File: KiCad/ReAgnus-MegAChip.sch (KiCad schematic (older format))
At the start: 19 parts, among them J3 Conn_02x01, J4 Conn_01x01, J5 Conn_01x01, J6 Conn_01x01, J7 Conn_01x01, U1 PLCC-84-Plug, U2 LM1117-3.3, U3 SN74CBTD16210, U4 SN74CBTD16210, U5 SN74CBTD16210, U6 SN74CBTD16210, U9 Agnus_TH_plug_pins

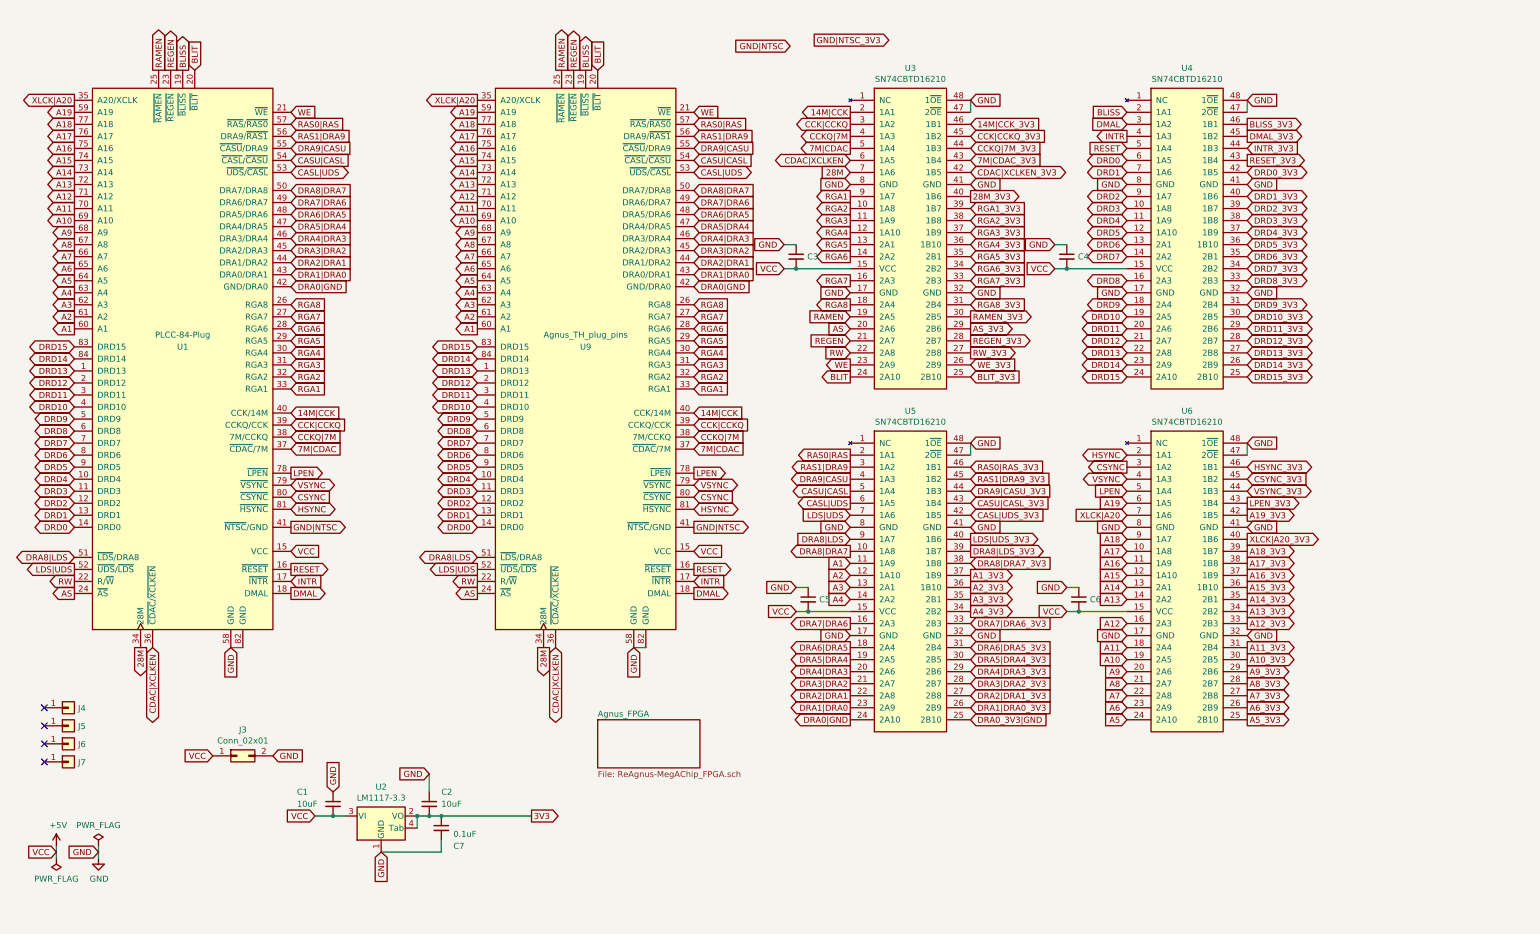
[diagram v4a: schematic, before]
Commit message: added 74LVC1G07 buffer with open-drain output
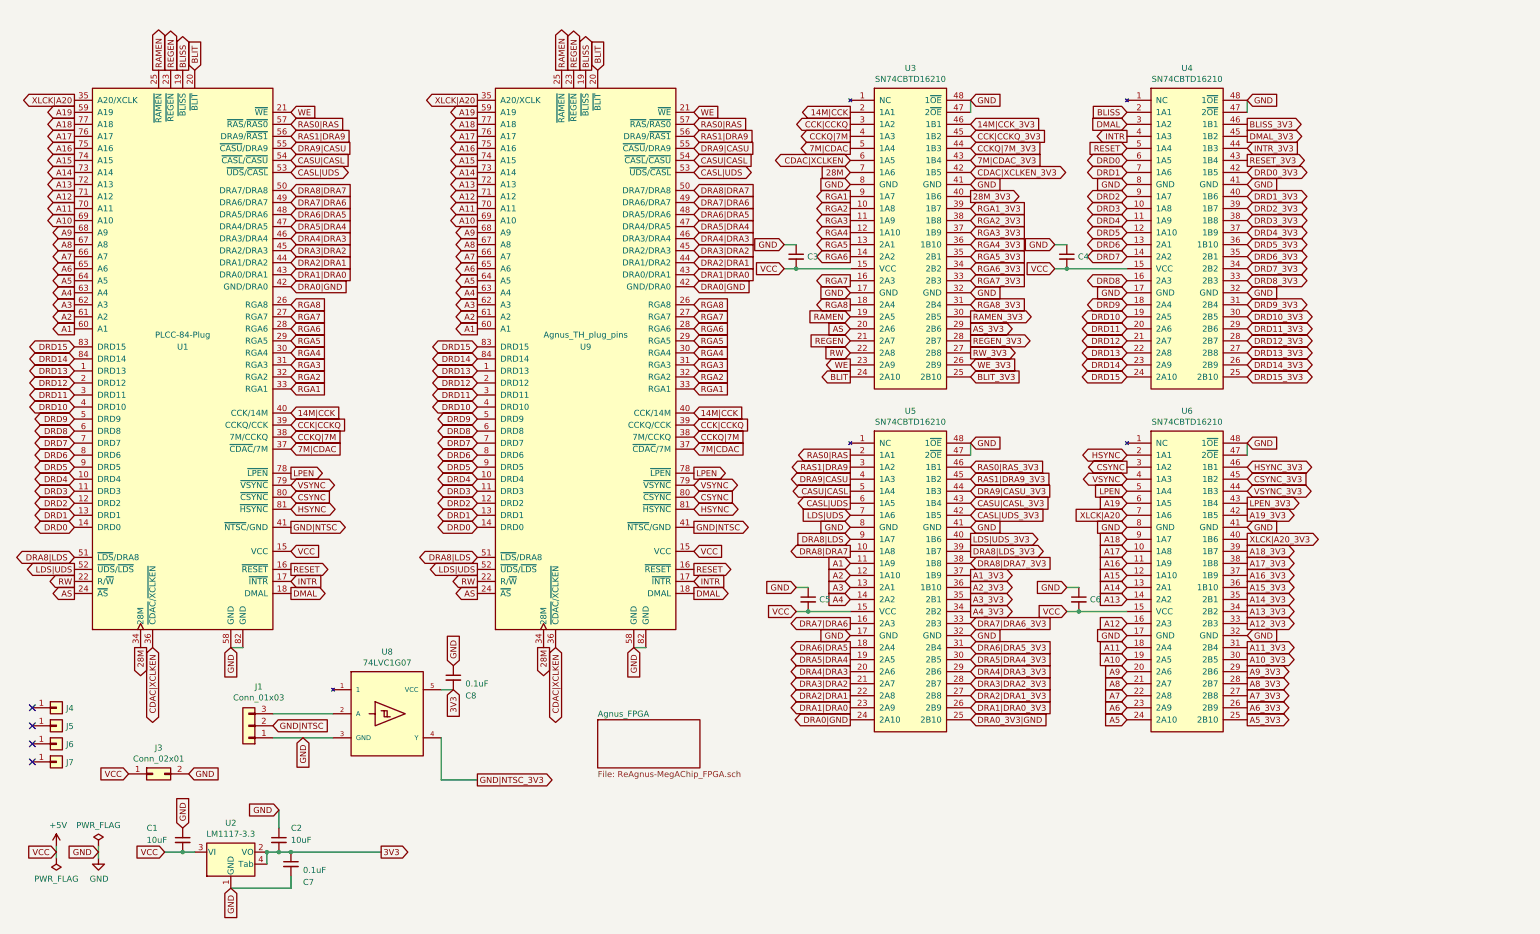
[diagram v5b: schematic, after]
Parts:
- added C8: 0.1uF, Capacitor_SMD:C_0805_2012Metric_Pad1.15x1.40mm_HandSolder, symbol Device:C_Small
- added J1: Conn_01x03, Connector_PinHeader_2.54mm:PinHeader_1x03_P2.54mm_Vertical, symbol Connector_Generic:Conn_01x03
- added U8: 74LVC1G07, Agnus:SOT-353_SC-70-5_Custom_Handsoldering, symbol ReAgnus-MegAChip:74LVC1G07
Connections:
- net 3V3: now also C8.2, U8.5 (VCC)
- net GND: now also C8.1, J1.1 (Pin_1), U8.3 (GND)
- net GND|NTSC: now also J1.2 (Pin_2)
- net GND|NTSC_3V3: now also U8.4 (Y)
- new net: J1.3 (Pin_3), U8.2 (A)
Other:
- moved on the sheet: C1, C2, C7, J3, J4, J5, J6, J7, U2
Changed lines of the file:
@@
 L Connector_Generic:Conn_01x01 J4
 U 1 1 60D1FBEB
-P 950 6200
-F 0 "J4" H 1030 6196 50  0000 L CNN
-F 1 "Conn_01x01" H 1030 6151 50  0001 L CNN
-F 2 "Connector_PinHeader_2.54mm:PinHeader_1x01_P2.54mm_Vertical" H 950 6200 50  0001 C CNN
-F 3 "~" H 950 6200 50  0001 C CNN
-	1    950  6200
+P 850 6200
+F 0 "J4" H 930 6196 50  0000 L CNN
+F 1 "Conn_01x01" H 930 6151 50  0001 L CNN
+F 2 "Connector_PinHeader_2.54mm:PinHeader_1x01_P2.54mm_Vertical" H 850 6200 50  0001 C CNN
+F 3 "~" H 850 6200 50  0001 C CNN
+	1    850  6200
 	1    0    0    -1
 $EndComp
@@
 L Connector_Generic:Conn_01x01 J5
 U 1 1 60D20CDD
-P 950 6350
-F 0 "J5" H 1030 6346 50  0000 L CNN
-F 1 "Conn_01x01" H 1030 6301 50  0001 L CNN
-F 2 "Connector_PinHeader_2.54mm:PinHeader_1x01_P2.54mm_Vertical" H 950 6350 50  0001 C CNN
-F 3 "~" H 950 6350 50  0001 C CNN
-	1    950  6350
+P 850 6350
+F 0 "J5" H 930 6346 50  0000 L CNN
+F 1 "Conn_01x01" H 930 6301 50  0001 L CNN
+F 2 "Connector_PinHeader_2.54mm:PinHeader_1x01_P2.54mm_Vertical" H 850 6350 50  0001 C CNN
+F 3 "~" H 850 6350 50  0001 C CNN
+	1    850  6350
 	1    0    0    -1
 $EndComp
@@
 L Connector_Generic:Conn_01x01 J6
 U 1 1 60D21648
-P 950 6500
-F 0 "J6" H 1030 6496 50  0000 L CNN
-F 1 "Conn_01x01" H 1030 6451 50  0001 L CNN
-F 2 "Connector_PinHeader_2.54mm:PinHeader_1x01_P2.54mm_Vertical" H 950 6500 50  0001 C CNN
-F 3 "~" H 950 6500 50  0001 C CNN
-	1    950  6500
+P 850 6500
+F 0 "J6" H 930 6496 50  0000 L CNN
+F 1 "Conn_01x01" H 930 6451 50  0001 L CNN
+F 2 "Connector_PinHeader_2.54mm:PinHeader_1x01_P2.54mm_Vertical" H 850 6500 50  0001 C CNN
+F 3 "~" H 850 6500 50  0001 C CNN
+	1    850  6500
 	1    0    0    -1
 $EndComp
@@
 L Connector_Generic:Conn_01x01 J7
 U 1 1 60D21D5E
-P 950 6650
-F 0 "J7" H 1030 6646 50  0000 L CNN
-F 1 "Conn_01x01" H 1030 6601 50  0001 L CNN
-F 2 "Connector_PinHeader_2.54mm:PinHeader_1x01_P2.54mm_Vertical" H 950 6650 50  0001 C CNN
-F 3 "~" H 950 6650 50  0001 C CNN
-	1    950  6650
-	1    0    0    -1
-$EndComp
-NoConn ~ 750  6200
-NoConn ~ 750  6350
-NoConn ~ 750  6500
-NoConn ~ 750  6650
+P 850 6650
+F 0 "J7" H 930 6646 50  0000 L CNN
+F 1 "Conn_01x01" H 930 6601 50  0001 L CNN
+F 2 "Connector_PinHeader_2.54mm:PinHeader_1x01_P2.54mm_Vertical" H 850 6650 50  0001 C CNN
+F 3 "~" H 850 6650 50  0001 C CNN
+	1    850  6650
+	1    0    0    -1
+$EndComp
+NoConn ~ 650  6200
+NoConn ~ 650  6350
+NoConn ~ 650  6500
+NoConn ~ 650  6650
 $Comp
 L Connector_Generic:Conn_02x01 J3
 U 1 1 60E54D12
-P 2350 6600
-F 0 "J3" H 2400 6817 50  0000 C CNN
-F 1 "Conn_02x01" H 2400 6726 50  0000 C CNN
-F 2 "Connector_PinHeader_2.54mm:PinHeader_2x01_P2.54mm_Vertical" H 2350 6600 50  0001 C CNN
-F 3 "~" H 2350 6600 50  0001 C CNN
-	1    2350 6600
-	1    0    0    -1
-$EndComp
-Text GLabel 2650 6600 2    50   Input ~ 0
+P 1650 6750
+F 0 "J3" H 1700 6967 50  0000 C CNN
+F 1 "Conn_02x01" H 1700 6876 50  0000 C CNN
+F 2 "Connector_PinHeader_2.54mm:PinHeader_2x01_P2.54mm_Vertical" H 1650 6750 50  0001 C CNN
+F 3 "~" H 1650 6750 50  0001 C CNN
+	1    1650 6750
+	1    0    0    -1
+$EndComp
+Text GLabel 1950 6750 2    50   Input ~ 0
 GND
 Wire Wire Line
@@
 L ReAgnus-MegAChip:LM1117-3.3 U2
 U 1 1 632C9030
-P 3550 7100
-F 0 "U2" H 3550 7342 50  0000 C CNN
-F 1 "LM1117-3.3" H 3550 7251 50  0000 C CNN
-F 2 "Package_TO_SOT_SMD:SOT-223" H 3550 7100 50  0001 C CNN
-F 3 "" H 3550 7100 50  0001 C CNN
-	1    3550 7100
+P 2300 7400
+F 0 "U2" H 2300 7642 50  0000 C CNN
+F 1 "LM1117-3.3" H 2300 7551 50  0000 C CNN
+F 2 "Package_TO_SOT_SMD:SOT-223" H 2300 7400 50  0001 C CNN
+F 3 "" H 2300 7400 50  0001 C CNN
+	1    2300 7400
 	1    0    0    -1
 $EndComp
@@
 Text GLabel 7450 1550 0    50   Output ~ 0
 7M|CDAC
-Text GLabel 7150 650  2    50   Output ~ 0
+Text GLabel 4350 6800 2    50   Output ~ 0
 GND|NTSC_3V3
 Text GLabel 4350 3200 0    50   BiDi ~ 0
@@
 Text GLabel 8450 6300 2    50   Input ~ 0
 DRA0_3V3|GND
-Text GLabel 6950 700  0    50   Input ~ 0
+Text GLabel 2650 6350 2    50   Input ~ 0
 GND|NTSC
-Text GLabel 3000 7100 0    50   Input ~ 0
+Text GLabel 1750 7400 0    50   Input ~ 0
 VCC
-Text GLabel 2150 6600 0    50   Input ~ 0
+Text GLabel 1450 6750 0    50   Input ~ 0
 VCC
-Text GLabel 3150 6900 1    50   Input ~ 0
+Text GLabel 1900 7200 1    50   Input ~ 0
 GND
 $Comp
 L Device:C_Small C2
 U 1 1 63947670
-P 3950 7000
+P 2700 7300
 AR Path="/63947670" Ref="C2"  Part="1"
 AR Path="/632D3BDF/63947670" Ref="C?"  Part="1"
 AR Path="/632F104D/63947670" Ref="C?"  Part="1"
-F 0 "C2" H 4050 7100 50  0000 L CNN
-F 1 "10uF" H 4050 7000 50  0000 L CNN
-F 2 "Capacitor_SMD:C_1206_3216Metric_Pad1.42x1.75mm_HandSolder" H 3950 7000 50  0001 C CNN
-F 3 "~" H 3950 7000 50  0001 C CNN
-	1    3950 7000
+F 0 "C2" H 2800 7400 50  0000 L CNN
+F 1 "10uF" H 2800 7300 50  0000 L CNN
+F 2 "Capacitor_SMD:C_1206_3216Metric_Pad1.42x1.75mm_HandSolder" H 2700 7300 50  0001 C CNN
+F 3 "~" H 2700 7300 50  0001 C CNN
+	1    2700 7300
 	1    0    0    -1
 $EndComp
@@
 L Device:C_Small C1
 U 1 1 63949338
-P 3150 7000
+P 1900 7300
 AR Path="/63949338" Ref="C1"  Part="1"
 AR Path="/632D3BDF/63949338" Ref="C?"  Part="1"
 AR Path="/632F104D/63949338" Ref="C?"  Part="1"
-F 0 "C1" H 2850 7100 50  0000 L CNN
-F 1 "10uF" H 2850 7000 50  0000 L CNN
-F 2 "Capacitor_SMD:C_1206_3216Metric_Pad1.42x1.75mm_HandSolder" H 3150 7000 50  0001 C CNN
-F 3 "~" H 3150 7000 50  0001 C CNN
-	1    3150 7000
-	1    0    0    -1
-$EndComp
-Wire Wire Line
-	3000 7100 3150 7100
-Connection ~ 3150 7100
-Wire Wire Line
-	3150 7100 3250 7100
-Text GLabel 3950 6750 0    50   Input ~ 0
-GND
-Wire Wire Line
-	3850 7100 3950 7100
-Wire Wire Line
-	3850 7200 3850 7100
-Connection ~ 3850 7100
-Text GLabel 4800 7100 2    50   Output ~ 0
+F 0 "C1" H 1600 7400 50  0000 L CNN
+F 1 "10uF" H 1600 7300 50  0000 L CNN
+F 2 "Capacitor_SMD:C_1206_3216Metric_Pad1.42x1.75mm_HandSolder" H 1900 7300 50  0001 C CNN
+F 3 "~" H 1900 7300 50  0001 C CNN
+	1    1900 7300
+	1    0    0    -1
+$EndComp
+Wire Wire Line
+	1750 7400 1900 7400
+Connection ~ 1900 7400
+Wire Wire Line
+	1900 7400 2000 7400
+Text GLabel 2700 7050 0    50   Input ~ 0
+GND
+Wire Wire Line
+	2600 7400 2700 7400
+Wire Wire Line
+	2600 7500 2600 7400
+Connection ~ 2600 7400
+Text GLabel 3550 7400 2    50   Output ~ 0
 3V3
-Connection ~ 3950 7100
-Wire Wire Line
-	3950 7100 4050 7100
-Text GLabel 3550 7400 3    50   Input ~ 0
+Connection ~ 2700 7400
+Wire Wire Line
+	2700 7400 2800 7400
+Text GLabel 2300 7700 3    50   Input ~ 0
 GND
 $Comp
 L Device:C_Small C7
 U 1 1 63951D9D
-P 4050 7200
+P 2800 7500
 AR Path="/63951D9D" Ref="C7"  Part="1"
 AR Path="/632D3BDF/63951D9D" Ref="C?"  Part="1"
 AR Path="/632F104D/63951D9D" Ref="C?"  Part="1"
-F 0 "C7" H 4150 7050 50  0000 L CNN
-F 1 "0.1uF" H 4150 7150 50  0000 L CNN
-F 2 "Capacitor_SMD:C_0805_2012Metric_Pad1.15x1.40mm_HandSolder" H 4050 7200 50  0001 C CNN
-F 3 "~" H 4050 7200 50  0001 C CNN
-	1    4050 7200
-	1    0    0    -1
-$EndComp
-Connection ~ 4050 7100
-Wire Wire Line
-	4050 7100 4800 7100
-Wire Wire Line
-	3950 6900 3950 6750
-Wire Wire Line
-	4050 7400 4050 7300
-Wire Wire Line
-	3550 7400 4050 7400
+F 0 "C7" H 2900 7350 50  0000 L CNN
+F 1 "0.1uF" H 2900 7450 50  0000 L CNN
+F 2 "Capacitor_SMD:C_0805_2012Metric_Pad1.15x1.40mm_HandSolder" H 2800 7500 50  0001 C CNN
+F 3 "~" H 2800 7500 50  0001 C CNN
+	1    2800 7500
+	1    0    0    -1
+$EndComp
+Connection ~ 2800 7400
+Wire Wire Line
+	2800 7400 3550 7400
+Wire Wire Line
+	2700 7200 2700 7050
+Wire Wire Line
+	2800 7700 2800 7600
+Wire Wire Line
+	2300 7700 2800 7700
+Wire Wire Line
+	4050 6800 4350 6800
+Wire Wire Line
+	4050 6450 4050 6800
+$Comp
+L ReAgnus-MegAChip:74LVC1G07 U8
+U 1 1 631A6F88
+P 3600 6250
+F 0 "U8" H 3600 6765 50  0000 C CNN
+F 1 "74LVC1G07" H 3600 6674 50  0000 C CNN
+F 2 "Agnus:SOT-353_SC-70-5_Custom_Handsoldering" H 4100 7200 50  0001 C CNN
+F 3 "https://www.ti.com/lit/ds/symlink/sn74lvc1g07-q1.pdf" H 4100 7200 50  0001 C CNN
+	1    3600 6250
+	1    0    0    -1
+$EndComp
+$Comp
+L Connector_Generic:Conn_01x03 J1
+U 1 1 631AE53C
+P 2450 6350
+F 0 "J1" H 2368 6025 50  0000 C CNN
+F 1 "Conn_01x03" H 2368 6116 50  0000 C CNN
+F 2 "Connector_PinHeader_2.54mm:PinHeader_1x03_P2.54mm_Vertical" H 2450 6350 50  0001 C CNN
+F 3 "~" H 2450 6350 50  0001 C CNN
+	1    2450 6350
+	-1   0    0    1
+$EndComp
+Wire Wire Line
+	3150 6250 2650 6250
+Wire Wire Line
+	3150 6450 2650 6450
+Text GLabel 2900 6450 3    50   Input ~ 0
+GND
+$Comp
+L Device:C_Small C8
+U 1 1 631B6BE4
+P 4150 5950
+AR Path="/631B6BE4" Ref="C8"  Part="1"
+AR Path="/632D3BDF/631B6BE4" Ref="C?"  Part="1"
+AR Path="/632F104D/631B6BE4" Ref="C?"  Part="1"
+F 0 "C8" H 4250 5800 50  0000 L CNN
+F 1 "0.1uF" H 4250 5900 50  0000 L CNN
+F 2 "Capacitor_SMD:C_0805_2012Metric_Pad1.15x1.40mm_HandSolder" H 4150 5950 50  0001 C CNN
+F 3 "~" H 4150 5950 50  0001 C CNN
+	1    4150 5950
+	1    0    0    -1
+$EndComp
+Text GLabel 4150 6050 3    50   Input ~ 0
+3V3
+Wire Wire Line
+	4050 6050 4150 6050
+Text GLabel 4150 5850 1    50   Input ~ 0
+GND
 $EndSCHEMATC

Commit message: more routing
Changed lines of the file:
@@
 Text GLabel 9750 4600 0    50   Input ~ 0
 XLCK|A20
-Text GLabel 7450 4800 0    50   Input ~ 0
+Text GLabel 7450 4800 0    50   BiDi ~ 0
 DRA8|LDS
-Text GLabel 7450 4600 0    50   Input ~ 0
-LDS|UDS
-Text GLabel 7450 4500 0    50   Output ~ 0
+Text GLabel 7450 4500 0    50   BiDi ~ 0
 CASL|UDS
 Text GLabel 7450 4300 0    50   Output ~ 0
@@
 Text GLabel 8450 4500 2    50   Input ~ 0
 CASU|CASL_3V3
-Text GLabel 8450 4600 2    50   Input ~ 0
+Text GLabel 8450 4600 2    50   BiDi ~ 0
 CASL|UDS_3V3
-Text GLabel 8450 4800 2    50   Output ~ 0
-LDS|UDS_3V3
-Text GLabel 8450 4900 2    50   Output ~ 0
+Text GLabel 8450 4900 2    50   BiDi ~ 0
 DRA8|LDS_3V3
 Text GLabel 8450 5000 2    50   Input ~ 0
@@
 Text GLabel 4150 5850 1    50   Input ~ 0
 GND
+Text GLabel 8450 4800 2    50   Output ~ 0
+LDS|UDS_3V3
+Text GLabel 7450 4600 0    50   Input ~ 0
+LDS|UDS
 $EndSCHEMATC

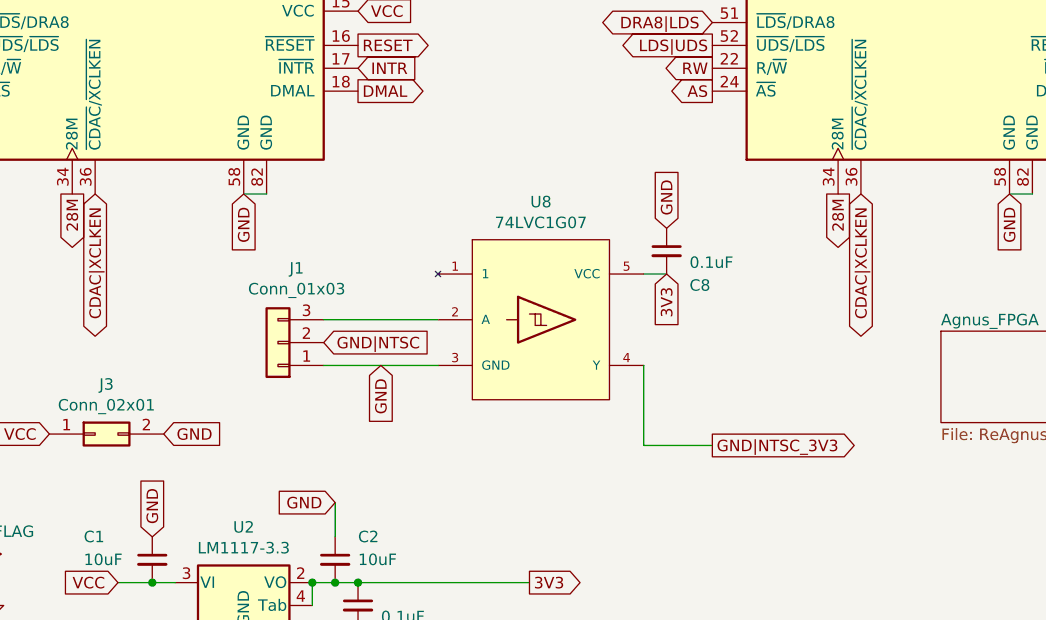
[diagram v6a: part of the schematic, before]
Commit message: added pull-up resistors on PAL/NTSC-line, added JTAG-header
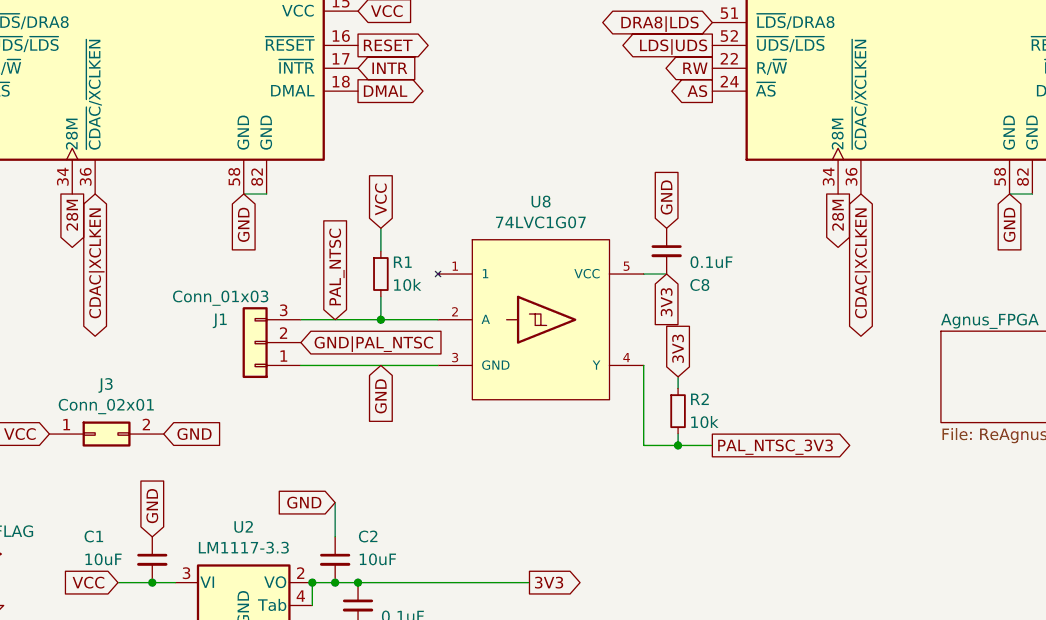
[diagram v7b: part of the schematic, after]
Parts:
- added R1, R2: 10k, Resistor_SMD:R_0603_1608Metric_Pad1.05x0.95mm_HandSolder, symbol Device:R_Small
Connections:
- net +5V: now also R1.1
- net 3V3: now also R2.1
- net GND|NTSC: no longer J1.2 (Pin_2)
- net PAL_NTSC: now reaches J1.3 (Pin_3), U8.2 (A)
- net PAL_NTSC: now also R1.2
- net GND|NTSC_3V3 renamed PAL_NTSC_3V3
- net PAL_NTSC_3V3: now also R2.2
- new net GND|PAL_NTSC: J1.2 (Pin_2)
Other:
- moved on the sheet: J1
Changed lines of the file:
@@
 7M|CDAC
 Text GLabel 4350 6800 2    50   Output ~ 0
-GND|NTSC_3V3
+PAL_NTSC_3V3
 Text GLabel 4350 3200 0    50   BiDi ~ 0
 DRD15
@@
 Text GLabel 8450 6300 2    50   Input ~ 0
 DRA0_3V3|GND
-Text GLabel 2650 6350 2    50   Input ~ 0
-GND|NTSC
+Text GLabel 2550 6350 2    50   Input ~ 0
+GND|PAL_NTSC
 Text GLabel 1750 7400 0    50   Input ~ 0
 VCC
@@
 	2300 7700 2800 7700
 Wire Wire Line
-	4050 6800 4350 6800
+	4050 6800 4200 6800
 Wire Wire Line
 	4050 6450 4050 6800
@@
 L Connector_Generic:Conn_01x03 J1
 U 1 1 631AE53C
-P 2450 6350
-F 0 "J1" H 2368 6025 50  0000 C CNN
-F 1 "Conn_01x03" H 2368 6116 50  0000 C CNN
-F 2 "Connector_PinHeader_2.54mm:PinHeader_1x03_P2.54mm_Vertical" H 2450 6350 50  0001 C CNN
-F 3 "~" H 2450 6350 50  0001 C CNN
-	1    2450 6350
+P 2350 6350
+F 0 "J1" H 2500 6250 50  0000 C CNN
+F 1 "Conn_01x03" H 2500 6150 50  0000 C CNN
+F 2 "Connector_PinHeader_2.54mm:PinHeader_1x03_P2.54mm_Vertical" H 2350 6350 50  0001 C CNN
+F 3 "~" H 2350 6350 50  0001 C CNN
+	1    2350 6350
 	-1   0    0    1
 $EndComp
 Wire Wire Line
-	3150 6250 2650 6250
-Wire Wire Line
-	3150 6450 2650 6450
+	3150 6250 2900 6250
 Text GLabel 2900 6450 3    50   Input ~ 0
 GND
@@
 Text GLabel 7450 4600 0    50   Input ~ 0
 LDS|UDS
+$Comp
+L Device:R_Small R1
+U 1 1 632802A6
+P 2900 6050
+F 0 "R1" H 2950 6100 50  0000 L CNN
+F 1 "10k" H 2950 6000 50  0000 L CNN
+F 2 "Resistor_SMD:R_0603_1608Metric_Pad1.05x0.95mm_HandSolder" H 2900 6050 50  0001 C CNN
+F 3 "~" H 2900 6050 50  0001 C CNN
+	1    2900 6050
+	1    0    0    -1
+$EndComp
+Connection ~ 2900 6250
+Text GLabel 4200 6500 1    50   Input ~ 0
+3V3
+Wire Wire Line
+	2900 6250 2900 6150
+Wire Wire Line
+	2900 5950 2900 5850
+Text GLabel 2700 6250 1    50   Input ~ 0
+PAL_NTSC
+Text GLabel 2900 5850 1    50   Input ~ 0
+VCC
+Wire Wire Line
+	2550 6250 2900 6250
+Wire Wire Line
+	2550 6450 3150 6450
+$Comp
+L Device:R_Small R2
+U 1 1 6328BA47
+P 4200 6650
+F 0 "R2" H 4250 6700 50  0000 L CNN
+F 1 "10k" H 4250 6600 50  0000 L CNN
+F 2 "Resistor_SMD:R_0603_1608Metric_Pad1.05x0.95mm_HandSolder" H 4200 6650 50  0001 C CNN
+F 3 "~" H 4200 6650 50  0001 C CNN
+	1    4200 6650
+	1    0    0    -1
+$EndComp
+Wire Wire Line
+	4200 6500 4200 6550
+Wire Wire Line
+	4200 6750 4200 6800
+Connection ~ 4200 6800
+Wire Wire Line
+	4200 6800 4350 6800
 $EndSCHEMATC
